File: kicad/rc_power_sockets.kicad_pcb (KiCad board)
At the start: 2 copper layers, 50 x 50 mm, 24 parts, among them IC1 ATTINY85, J1 PIR, J2 433MHZ, J3 433MHZ, P1 ICSP, P2 POWER_CONNECTION, Q1 NMOS, Q2 PMOS, U1 MCP1700T

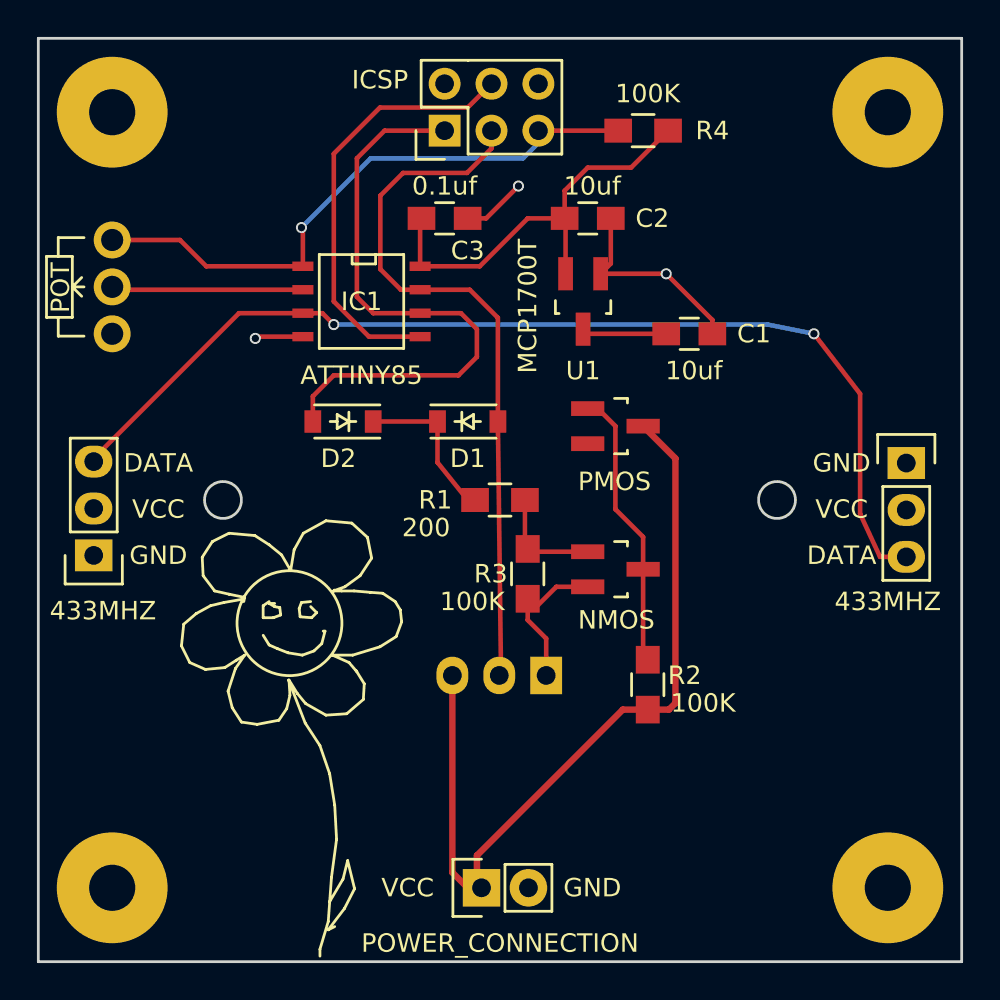
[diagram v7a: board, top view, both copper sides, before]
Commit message: M3 mounting holes
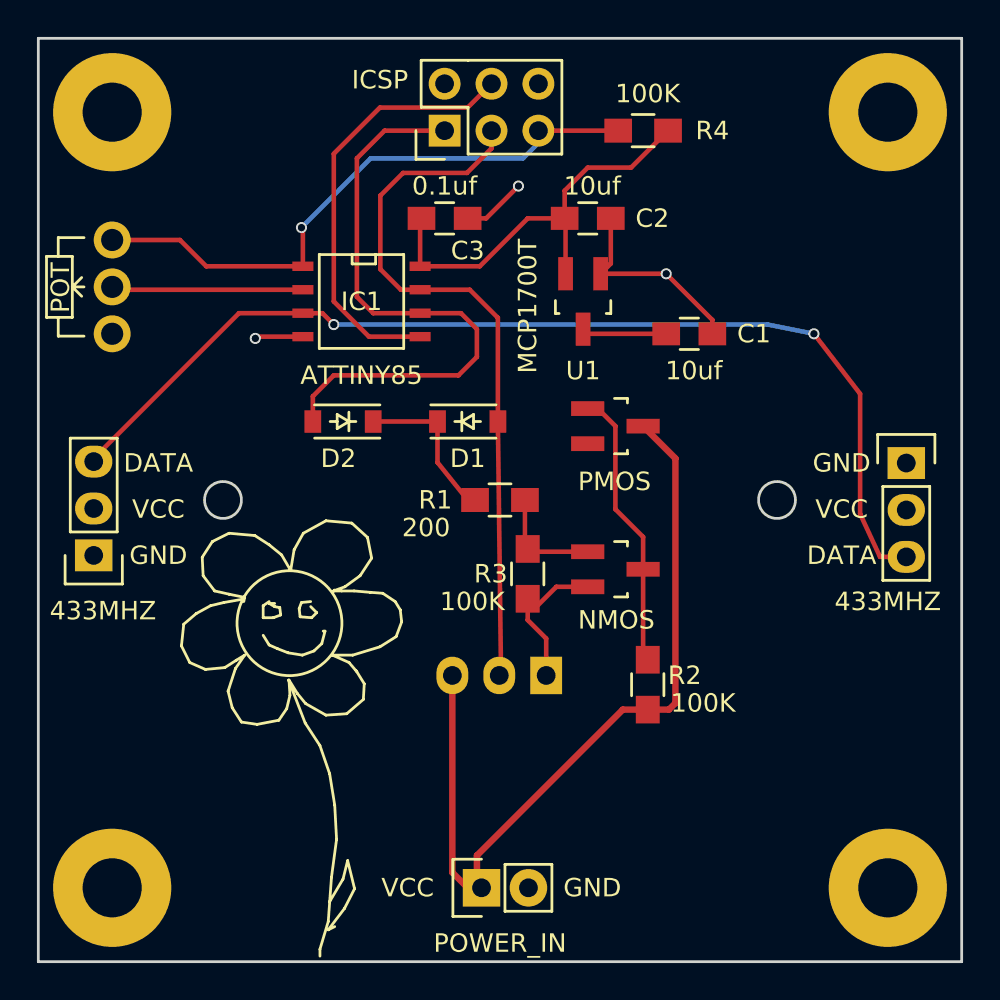
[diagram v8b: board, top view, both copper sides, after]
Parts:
- D1, D2: value D -> D_Schottky
- MOUNT1, MOUNT2, MOUNT3, MOUNT4: footprint Wire_Pads:SolderWirePad_single_2-5mmDrill -> Mounting_Holes:MountingHole_3.2mm_M3_Pad
- P2: value POWER_CONNECTION -> POWER_IN
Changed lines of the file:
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@@
       (effects (font (size 1 1) (thickness 0.15)))
     )
-    (fp_text value D (at 0 2.1) (layer F.Fab) hide
+    (fp_text value D_Schottky (at 0 2.1) (layer F.Fab) hide
       (effects (font (size 1 1) (thickness 0.15)))
     )
@@
       (effects (font (size 1 1) (thickness 0.15)))
     )
-    (fp_text value D (at 0 2.1 180) (layer F.Fab) hide
+    (fp_text value D_Schottky (at 0 2.1 180) (layer F.Fab) hide
       (effects (font (size 1 1) (thickness 0.15)))
     )
@@
     )
   )
-  (module Wire_Pads:SolderWirePad_single_2-5mmDrill (layer F.Cu)
-    (at 166 106)
-    (fp_text reference MOUNT1 (at -6 2.5) (layer F.SilkS) hide
-      (effects (font (size 1 1) (thickness 0.15)))
-    )
-    (fp_text value CONN_01X01 (at 1.27 5.08) (layer F.Fab) hide
-      (effects (font (size 1 1) (thickness 0.15)))
-    )
-    (pad 1 thru_hole circle (at 0 0) (size 5.99948 5.99948) (drill 2.49936) (layers *.Cu *.Mask F.SilkS)
-      (net 1 GND))
-  )
-  (module Wire_Pads:SolderWirePad_single_2-5mmDrill (layer F.Cu)
-    (at 124 106)
-    (fp_text reference MOUNT2 (at 6 2.5) (layer F.SilkS) hide
-      (effects (font (size 1 1) (thickness 0.15)))
-    )
-    (fp_text value CONN_01X01 (at 1.27 5.08) (layer F.Fab) hide
-      (effects (font (size 1 1) (thickness 0.15)))
-    )
-    (pad 1 thru_hole circle (at 0 0) (size 5.99948 5.99948) (drill 2.49936) (layers *.Cu *.Mask F.SilkS)
-      (net 1 GND))
-  )
-  (module Wire_Pads:SolderWirePad_single_2-5mmDrill (layer F.Cu)
-    (at 166 64)
-    (fp_text reference MOUNT3 (at -6 -2.5) (layer F.SilkS) hide
-      (effects (font (size 1 1) (thickness 0.15)))
-    )
-    (fp_text value CONN_01X01 (at 1.27 5.08) (layer F.Fab) hide
-      (effects (font (size 1 1) (thickness 0.15)))
-    )
-    (pad 1 thru_hole circle (at 0 0) (size 5.99948 5.99948) (drill 2.49936) (layers *.Cu *.Mask F.SilkS)
-      (net 1 GND))
-  )
-  (module Wire_Pads:SolderWirePad_single_2-5mmDrill (layer F.Cu)
-    (at 124 64)
-    (fp_text reference MOUNT4 (at 6 -2.5) (layer F.SilkS) hide
-      (effects (font (size 1 1) (thickness 0.15)))
-    )
-    (fp_text value CONN_01X01 (at 1.27 5.08 90) (layer F.Fab) hide
-      (effects (font (size 1 1) (thickness 0.15)))
-    )
-    (pad 1 thru_hole circle (at 0 0) (size 5.99948 5.99948) (drill 2.49936) (layers *.Cu *.Mask F.SilkS)
-      (net 1 GND))
-  )
   (module Pin_Headers:Pin_Header_Straight_1x02 (layer F.Cu)
     (at 144 106 90)
@@
       (effects (font (size 1 1) (thickness 0.15)))
     )
-    (fp_text value POWER_CONNECTION (at -3 1 180) (layer F.SilkS)
+    (fp_text value POWER_IN (at -3 1 180) (layer F.SilkS)
       (effects (font (size 1 1) (thickness 0.15)))
     )
@@
     (fp_circle (center 0.4 6.87) (end 2.94 5.6) (layer F.SilkS) (width 0.15))
   )
+  (module Mounting_Holes:MountingHole_3.2mm_M3_Pad (layer F.Cu)
+    (at 166 106)
+    (descr "Mounting Hole 3.2mm, M3")
+    (tags "mounting hole 3.2mm m3")
+    (fp_text reference MOUNT1 (at 0 -4.2) (layer F.SilkS) hide
+      (effects (font (size 1 1) (thickness 0.15)))
+    )
+    (fp_text value CONN_01X01 (at 0 4.2) (layer F.Fab) hide
+      (effects (font (size 1 1) (thickness 0.15)))
+    )
+    (fp_circle (center 0 0) (end 3.2 0) (layer Cmts.User) (width 0.15))
+    (fp_circle (center 0 0) (end 3.45 0) (layer F.CrtYd) (width 0.05))
+    (pad 1 thru_hole circle (at 0 0) (size 6.4 6.4) (drill 3.2) (layers *.Cu *.Mask F.SilkS)
+      (net 1 GND))
+  )
+  (module Mounting_Holes:MountingHole_3.2mm_M3_Pad (layer F.Cu)
+    (at 124 106)
+    (descr "Mounting Hole 3.2mm, M3")
+    (tags "mounting hole 3.2mm m3")
+    (fp_text reference MOUNT2 (at 0 -4.2) (layer F.SilkS) hide
+      (effects (font (size 1 1) (thickness 0.15)))
+    )
+    (fp_text value CONN_01X01 (at 0 4.2) (layer F.Fab) hide
+      (effects (font (size 1 1) (thickness 0.15)))
+    )
+    (fp_circle (center 0 0) (end 3.2 0) (layer Cmts.User) (width 0.15))
+    (fp_circle (center 0 0) (end 3.45 0) (layer F.CrtYd) (width 0.05))
+    (pad 1 thru_hole circle (at 0 0) (size 6.4 6.4) (drill 3.2) (layers *.Cu *.Mask F.SilkS)
+      (net 1 GND))
+  )
+  (module Mounting_Holes:MountingHole_3.2mm_M3_Pad (layer F.Cu)
+    (at 166 64)
+    (descr "Mounting Hole 3.2mm, M3")
+    (tags "mounting hole 3.2mm m3")
+    (fp_text reference MOUNT3 (at 0 -4.2) (layer F.SilkS) hide
+      (effects (font (size 1 1) (thickness 0.15)))
+    )
+    (fp_text value CONN_01X01 (at 0 4.2) (layer F.Fab) hide
+      (effects (font (size 1 1) (thickness 0.15)))
+    )
+    (fp_circle (center 0 0) (end 3.2 0) (layer Cmts.User) (width 0.15))
+    (fp_circle (center 0 0) (end 3.45 0) (layer F.CrtYd) (width 0.05))
+    (pad 1 thru_hole circle (at 0 0) (size 6.4 6.4) (drill 3.2) (layers *.Cu *.Mask F.SilkS)
+      (net 1 GND))
+  )
+  (module Mounting_Holes:MountingHole_3.2mm_M3_Pad (layer F.Cu)
+    (at 124 64)
+    (descr "Mounting Hole 3.2mm, M3")
+    (tags "mounting hole 3.2mm m3")
+    (fp_text reference MOUNT4 (at 0 -4.2) (layer F.SilkS) hide
+      (effects (font (size 1 1) (thickness 0.15)))
+    )
+    (fp_text value CONN_01X01 (at 0 4.2) (layer F.Fab) hide
+      (effects (font (size 1 1) (thickness 0.15)))
+    )
+    (fp_circle (center 0 0) (end 3.2 0) (layer Cmts.User) (width 0.15))
+    (fp_circle (center 0 0) (end 3.45 0) (layer F.CrtYd) (width 0.05))
+    (pad 1 thru_hole circle (at 0 0) (size 6.4 6.4) (drill 3.2) (layers *.Cu *.Mask F.SilkS)
+      (net 1 GND))
+  )
   (gr_text www.theapi.co.uk (at 144.8 82.6) (layer B.SilkS)
